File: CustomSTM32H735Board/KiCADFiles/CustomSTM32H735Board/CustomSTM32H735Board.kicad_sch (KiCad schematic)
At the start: 95 parts, among them IC1 NCP700BSN33T1G, J1 Conn_01x03_Socket, J2 FTSH-105-01-L-DV-K, J3 FLE-125-01-G-DV, SW1 SW_Omron_B3FS, U1 L7805, U2 OPA1678IDGKT, U3 STM32H735IGT6, X1 NSC5004A-25M

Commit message: Layout finished. Started with board design of custom board.
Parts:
- removed J1: Conn_01x03_Socket, Connector_JST:JST_XH_B3B-XH-A_1x03_P2.50mm_Vertical, symbol Connector:Conn_01x03_Socket
- added JP4: SolderJumper_3_Open, Jumper:SolderJumper-3_P1.3mm_Open_Pad1.0x1.5mm_NumberLabels, symbol Jumper:SolderJumper_3_Open
- added TP1, TP2, TP3, TP5: TestPoint, Connector_Pin:Pin_D0.7mm_L6.5mm_W1.8mm_FlatFork, symbol Connector:TestPoint
- renumbered C9 to C10, C10 to C9, J3 to J1, J2 to JSWD1, TP1 to TP4
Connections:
- net VDD is gone; now on net +3.3V: C11.1, C16.1, C20.1, FB1.1, JP3.1 (A), U3.105, U3.113, U3.126, U3.13, U3.136, U3.152, U3.160, U3.176, U3.25, U3.44, U3.48, U3.65, U3.7, U3.71, U3.8, U3.84, U3.92, U3.99, UHYPERRAM1.B4 (VCC), UHYPERRAM1.D1 (VCCQ), UHYPERRAM1.E4 (VCCQ)
- net VSS is gone; now on net GND: U3.100, U3.106, U3.112, U3.119, U3.12, U3.121, U3.134, U3.137, U3.151, U3.159, U3.173, U3.24, U3.38, U3.45, U3.47, U3.6, U3.64, U3.70, U3.81, U3.83, U3.93, UHYPERRAM1.B3 (VSS), UHYPERRAM1.C1 (VSSQ), UHYPERRAM1.E5 (VSSQ)
- net +3.3V: now also TP3.1
- net +5V: now also TP1.1
- net -5V: now also TP2.1
- net NRST: now also JP4.1 (A), TP5.1; no longer J1.36
- net PD0: now reaches U3.143
- net PD0: now also JP4.3 (B)
- new net: J1.36, JP4.2 (C)
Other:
- note added: "LCD TFT pinout equal to the DK board: CTP_INT: PG2 (39) LCD_BL_CTRL: PG15 (43) LCD_RST: instead of PH6 new PD0(36) LCD_DISP: PD10 (24)"
- note added: "imported design rules PCBWay: Std: track width: 0.1524 via diam: 0.4572 via hole: 0.254 Minimals: track width: 0.1016 via diam: 0.2 via hole: 0.1"
- note removed: "package size / footprint?"
- moved on the sheet: C8, C9, SW1

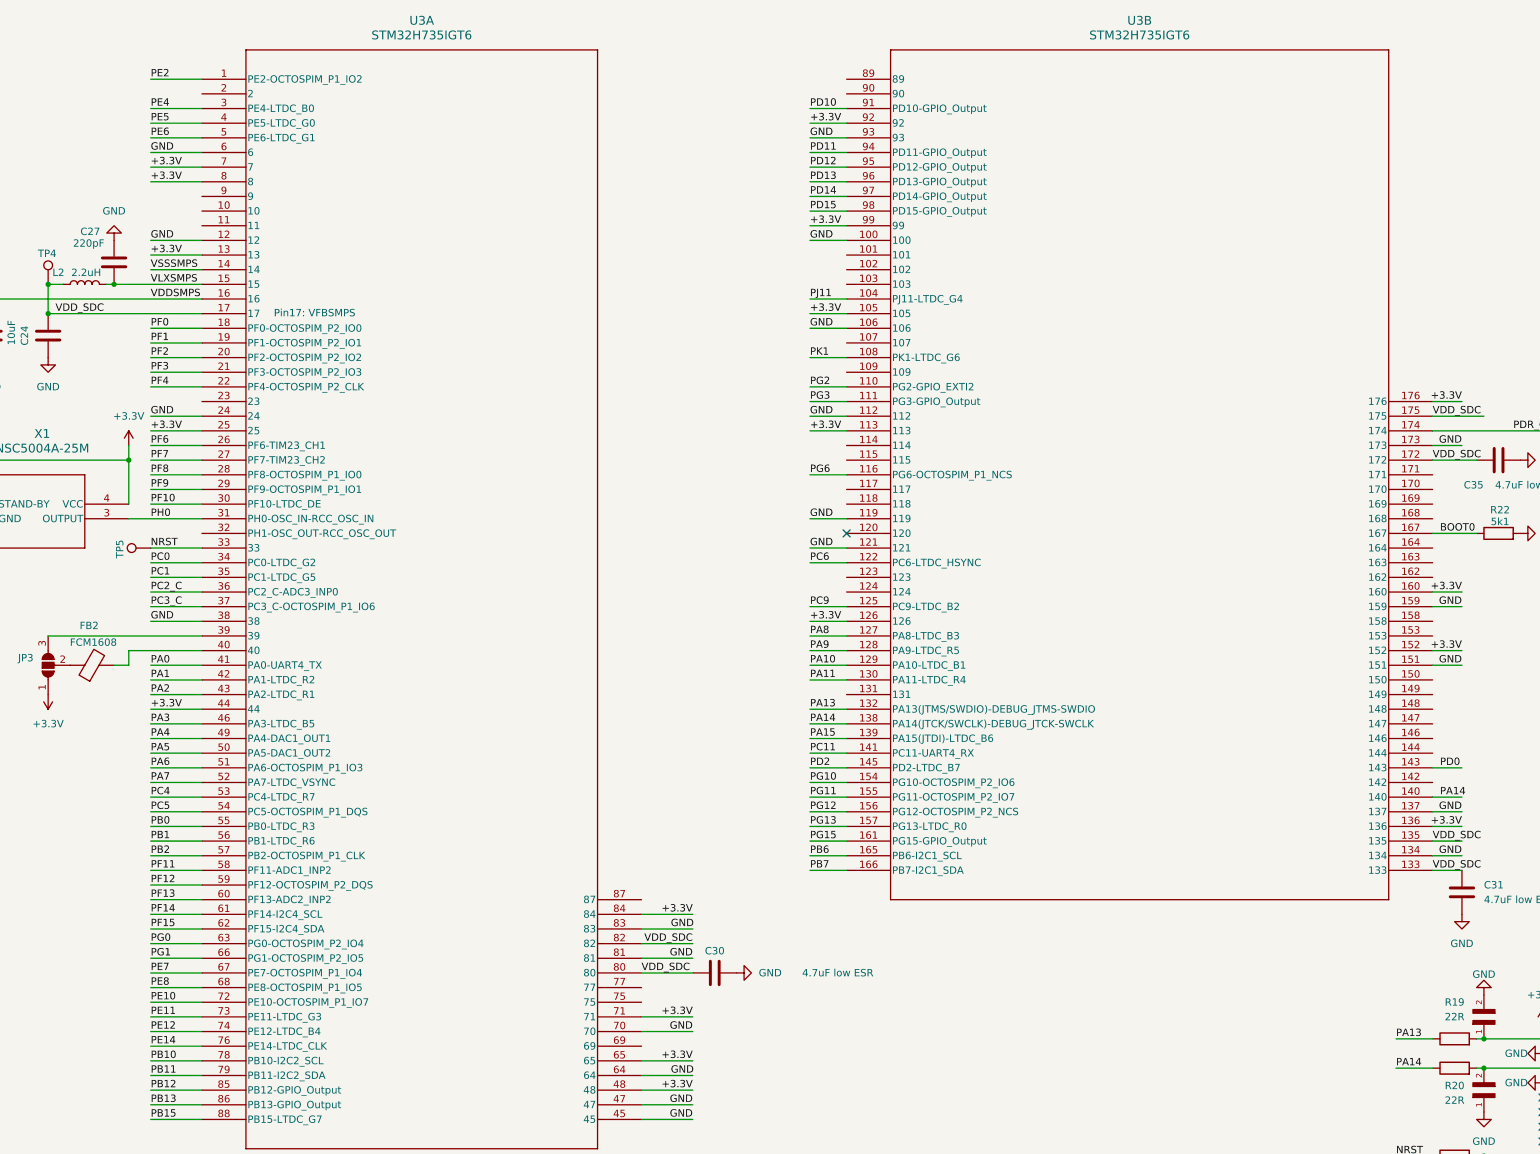
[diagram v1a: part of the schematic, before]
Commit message: work on layout, first possible solution
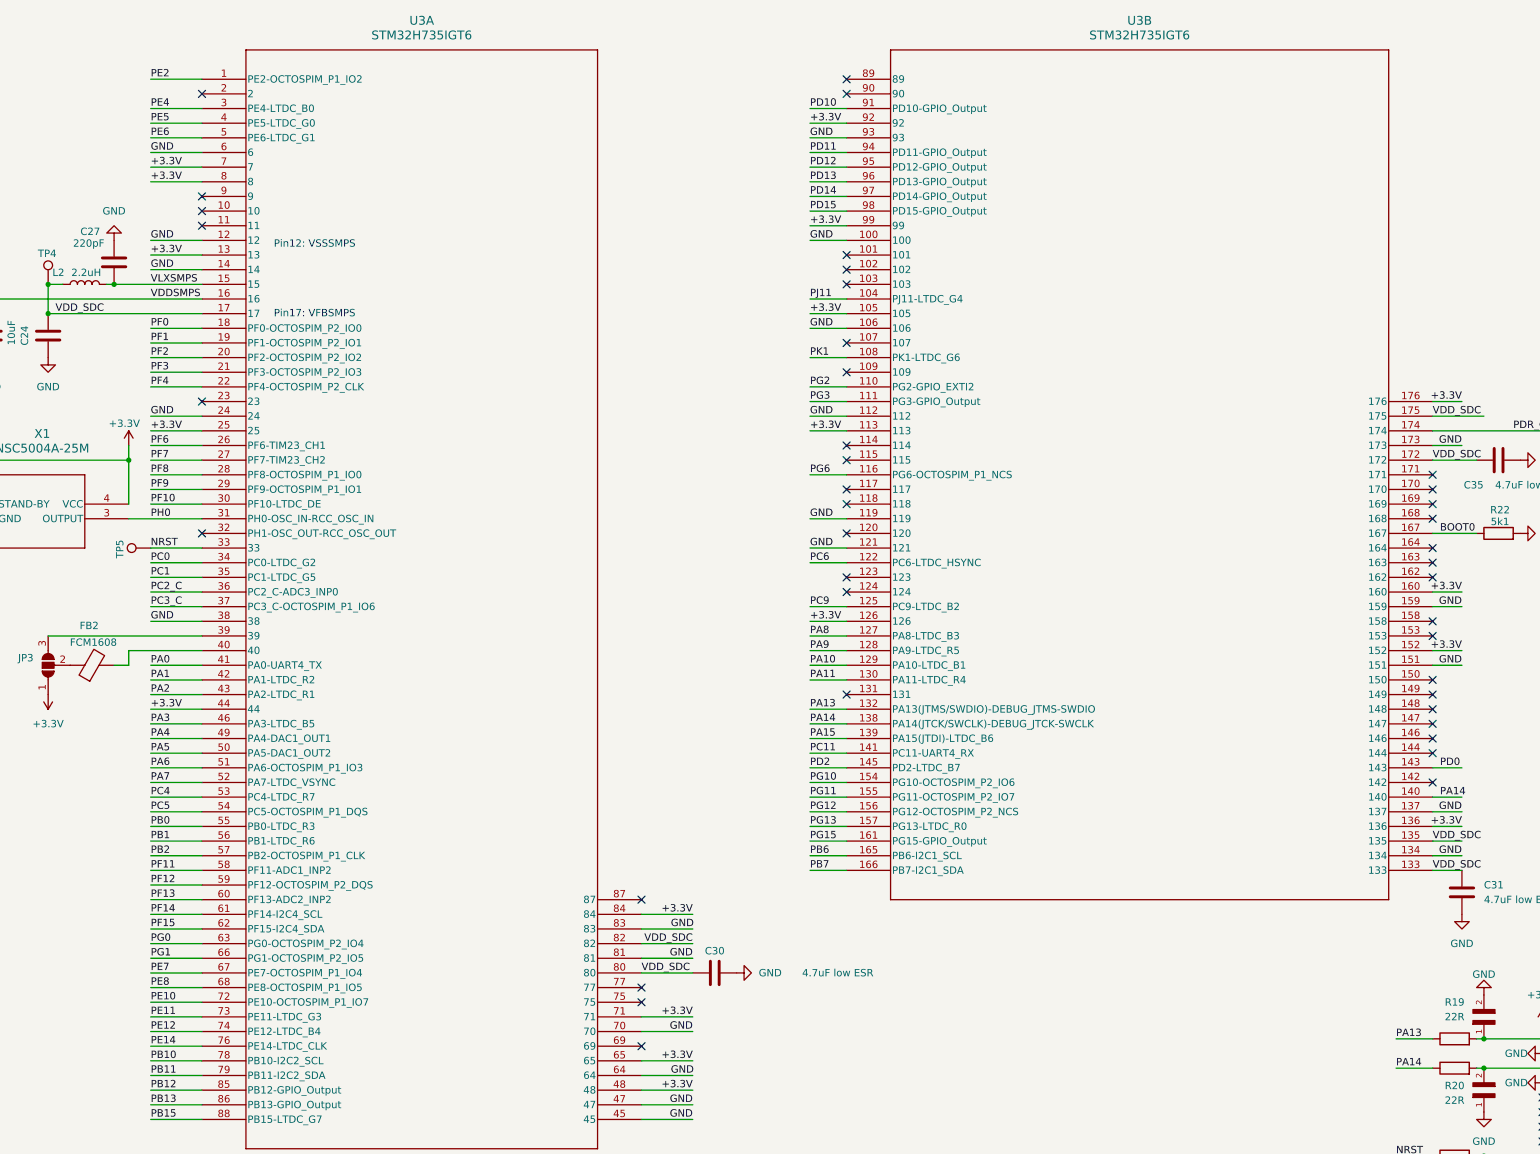
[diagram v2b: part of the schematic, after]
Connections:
- net VSSSMPS is gone; now on net GND: U3.14
- no-connect marks 18 -> 58
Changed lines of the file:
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@@
 	)
 	(no_connect
+		(at 419.1 152.4)
+	)
+	(no_connect
 		(at 438.15 242.57)
 	)
 	(no_connect
+		(at 317.5 58.42)
+	)
+	(no_connect
+		(at 317.5 121.92)
+	)
+	(no_connect
+		(at 317.5 144.78)
+	)
+	(no_connect
+		(at 419.1 139.7)
+	)
+	(no_connect
+		(at 317.5 109.22)
+	)
+	(no_connect
 		(at 86.36 284.48)
 	)
 	(no_connect
+		(at 419.1 162.56)
+	)
+	(no_connect
+		(at 419.1 170.18)
+	)
+	(no_connect
 		(at 80.01 147.32)
 	)
 	(no_connect
+		(at 317.5 104.14)
+	)
+	(no_connect
+		(at 317.5 124.46)
+	)
+	(no_connect
+		(at 419.1 180.34)
+	)
+	(no_connect
 		(at 317.5 137.16)
 	)
@@
 	)
 	(no_connect
+		(at 419.1 142.24)
+	)
+	(no_connect
+		(at 317.5 132.08)
+	)
+	(no_connect
+		(at 419.1 167.64)
+	)
+	(no_connect
+		(at 317.5 88.9)
+	)
+	(no_connect
+		(at 317.5 147.32)
+	)
+	(no_connect
 		(at 125.73 172.72)
 	)
 	(no_connect
+		(at 419.1 132.08)
+	)
+	(no_connect
+		(at 317.5 129.54)
+	)
+	(no_connect
 		(at 85.09 120.65)
 	)
 	(no_connect
+		(at 317.5 93.98)
+	)
+	(no_connect
 		(at 438.15 234.95)
 	)
 	(no_connect
+		(at 419.1 154.94)
+	)
+	(no_connect
+		(at 281.94 215.9)
+	)
+	(no_connect
+		(at 205.74 83.82)
+	)
+	(no_connect
 		(at 438.15 237.49)
 	)
 	(no_connect
+		(at 317.5 91.44)
+	)
+	(no_connect
 		(at 80.01 154.94)
 	)
 	(no_connect
+		(at 205.74 81.28)
+	)
+	(no_connect
+		(at 281.94 218.44)
+	)
+	(no_connect
 		(at 80.01 167.64)
 	)
 	(no_connect
+		(at 419.1 127)
+	)
+	(no_connect
 		(at 438.15 240.03)
 	)
@@
 	)
 	(no_connect
+		(at 419.1 175.26)
+	)
+	(no_connect
+		(at 419.1 144.78)
+	)
+	(no_connect
 		(at 85.09 118.11)
 	)
 	(no_connect
+		(at 205.74 137.16)
+	)
+	(no_connect
+		(at 205.74 114.3)
+	)
+	(no_connect
+		(at 419.1 129.54)
+	)
+	(no_connect
 		(at 478.79 175.26)
 	)
@@
 	)
 	(no_connect
+		(at 419.1 172.72)
+	)
+	(no_connect
+		(at 317.5 60.96)
+	)
+	(no_connect
+		(at 317.5 165.1)
+	)
+	(no_connect
+		(at 281.94 226.06)
+	)
+	(no_connect
+		(at 419.1 134.62)
+	)
+	(no_connect
 		(at 478.79 162.56)
 	)
 	(no_connect
+		(at 419.1 165.1)
+	)
+	(no_connect
+		(at 205.74 60.96)
+	)
+	(no_connect
+		(at 281.94 200.66)
+	)
+	(no_connect
+		(at 205.74 78.74)
+	)
+	(no_connect
 		(at 478.79 180.34)
 	)
@@
 		)
 	)
+	(text_box "Pin12: VSSSMPS"
+		(exclude_from_sim no)
+		(at 217.17 85.09 0)
+		(size 18.415 2.54)
+		(stroke
+			(width -0.0001)
+			(type default)
+		)
+		(fill
+			(type color)
+			(color 0 0 0 0)
+		)
+		(effects
+			(font
+				(size 1.27 1.27)
+			)
+			(justify left top)
+		)
+	)
 	(text "DAC1:\n2: OUT1	PA4\n3: OUT2	PA5"
 		(exclude_from_sim no)
@@
 		)
 	)
-	(label "VSSSMPS"
-		(at 196.85 91.44 0)
-		(fields_autoplaced yes)
-		(effects
-			(font
-				(size 1.27 1.27)
-			)
-			(justify left bottom)
-		)
-	)
 	(label "PF2"
 		(at 196.85 106.68 0)
@@
 		)
 	)
+	(label "GND"
+		(at 196.85 91.44 0)
+		(fields_autoplaced yes)
+		(effects
+			(font
+				(size 1.27 1.27)
+			)
+			(justify left bottom)
+		)
+	)
 	(label "PB13"
 		(at 196.85 236.22 0)
@@
 		)
 		(property "Value" "+3.3V"
-			(at 193.04 116.84 0)
+			(at 192.278 118.11 0)
 			(effects
 				(font
